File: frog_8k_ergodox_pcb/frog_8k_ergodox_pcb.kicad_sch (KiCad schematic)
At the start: 214 parts, among them J1 USB_C_Receptacle_USB2.0_14P, J10 Conn_01x01_Pin, J2 Conn_01x04_Pin, J3 Conn_01x01_Pin, J4 Conn_01x01_Pin, J5 Conn_01x01_Pin, J6 Conn_01x01_Pin, J7 Conn_01x01_Pin, J8 Conn_01x01_Pin, J9 Conn_01x01_Pin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

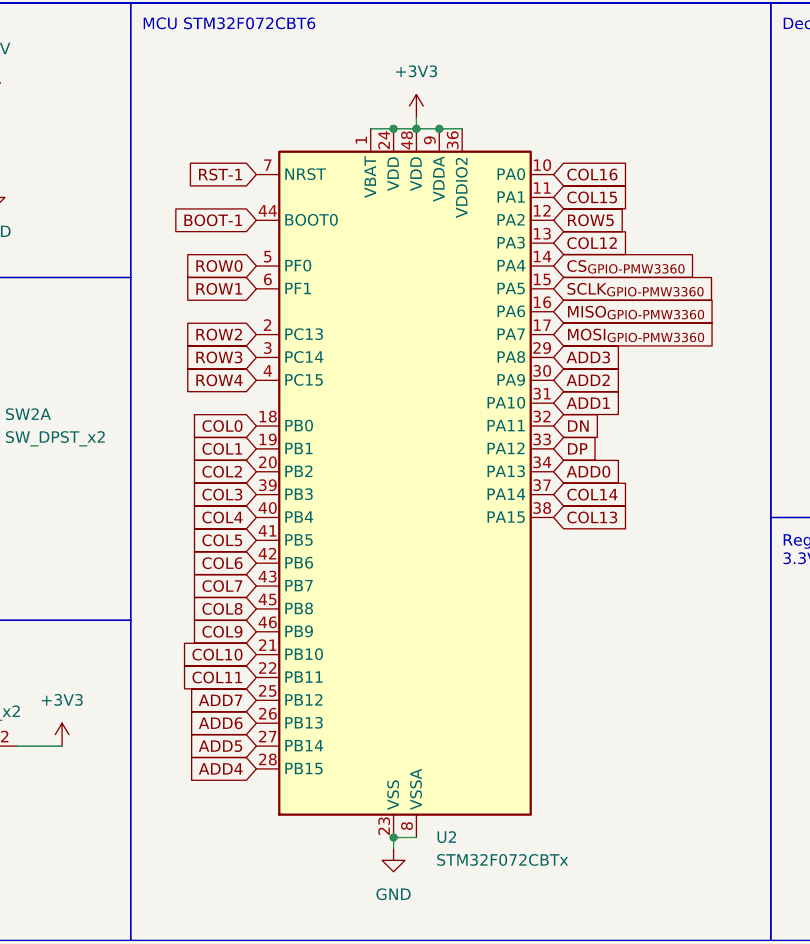
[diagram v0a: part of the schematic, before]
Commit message: Connected All nets.
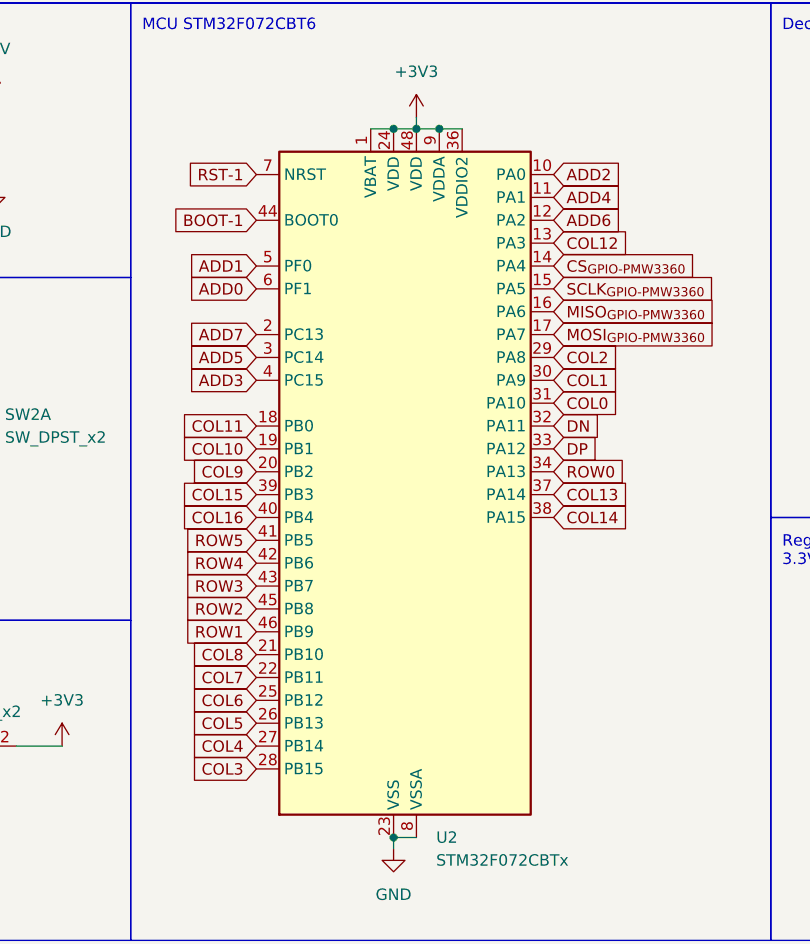
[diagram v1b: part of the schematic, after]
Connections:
- net ADD0: now also U2.6 (PF1); no longer U2.34 (PA13)
- net ADD1: now also U2.5 (PF0); no longer U2.31 (PA10)
- net ADD2: now also U2.10 (PA0); no longer U2.30 (PA9)
- net ADD3: now also U2.4 (PC15); no longer U2.29 (PA8)
- net ADD4: now also U2.11 (PA1); no longer U2.28 (PB15)
- net ADD5: now also U2.3 (PC14); no longer U2.27 (PB14)
- net ADD6: now also U2.12 (PA2); no longer U2.26 (PB13)
- net ADD7: now also U2.2 (PC13); no longer U2.25 (PB12)
- net COL0: now also U2.31 (PA10); no longer U2.18 (PB0)
- net COL1: now also U2.30 (PA9); no longer U2.19 (PB1)
- net COL10: now also U2.19 (PB1); no longer U2.21 (PB10)
- net COL11: now also U2.18 (PB0); no longer U2.22 (PB11)
- net COL13: now also U2.37 (PA14); no longer U2.38 (PA15)
- net COL14: now also U2.38 (PA15); no longer U2.37 (PA14)
- net COL15: now also U2.39 (PB3); no longer U2.11 (PA1)
- net COL16: now also U2.40 (PB4); no longer U2.10 (PA0)
- net COL2: now also U2.29 (PA8); no longer U2.20 (PB2)
- net COL3: now also U2.28 (PB15); no longer U2.39 (PB3)
- net COL4: now also U2.27 (PB14); no longer U2.40 (PB4)
- net COL5: now also U2.26 (PB13); no longer U2.41 (PB5)
- net COL6: now also U2.25 (PB12); no longer U2.42 (PB6)
- net COL7: now also U2.22 (PB11); no longer U2.43 (PB7)
- net COL8: now also U2.21 (PB10); no longer U2.45 (PB8)
- net COL9: now also U2.20 (PB2); no longer U2.46 (PB9)
- net ROW0: now also U2.34 (PA13); no longer U2.5 (PF0)
- net ROW1: now also U2.46 (PB9); no longer U2.6 (PF1)
- net ROW2: now also U2.45 (PB8); no longer U2.2 (PC13)
- net ROW3: now also U2.43 (PB7); no longer U2.3 (PC14)
- net ROW4: now also U2.42 (PB6); no longer U2.4 (PC15)
- net ROW5: now also U2.41 (PB5); no longer U2.12 (PA2)

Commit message: Almost Done with pcb
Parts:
- added R4: R1_10k, Resistor_SMD:R_0805_2012Metric_Pad1.20x1.40mm_HandSolder, symbol Device:R
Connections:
- no-connect marks 4 -> 6
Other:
- note added: "Additional Capacitor"
- note added: "Additional Resistor"
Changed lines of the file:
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@@
 	)
 	(no_connect
+		(at 326.39 77.47)
+	)
+	(no_connect
+		(at 334.01 77.47)
+	)
+	(no_connect
 		(at 270.51 261.62)
 	)
@@
 	)
 	(rectangle
+		(start 323.85 60.96)
+		(end 365.76 99.06)
+		(stroke
+			(width 0)
+			(type default)
+		)
+		(fill
+			(type none)
+		)
+	)
+	(rectangle
 		(start 212.09 237.49)
 		(end 299.72 284.48)
@@
 		)
 	)
+	(rectangle
+		(start 365.76 60.96)
+		(end 407.67 99.06)
+		(stroke
+			(width 0)
+			(type default)
+		)
+		(fill
+			(type none)
+		)
+	)
 	(text "TrackBall Housing\nMounting Hole, M2"
 		(exclude_from_sim no)
@@
 		)
 	)
+	(text "Additional Resistor"
+		(exclude_from_sim no)
+		(at 325.12 63.5 0)
+		(effects
+			(font
+				(size 1.27 1.27)
+			)
+			(justify left)
+		)
+	)
 	(text "MCU STM32F072CBT6"
 		(exclude_from_sim no)
@@
 		)
 	)
+	(text "Additional Capacitor"
+		(exclude_from_sim no)
+		(at 367.03 63.5 0)
+		(effects
+			(font
+				(size 1.27 1.27)
+			)
+			(justify left)
+		)
+	)
 	(text "Boot Switch\n"
 		(exclude_from_sim no)
@@
 					(unit 1)
 				)
+			)
+		)
+	)
+	(symbol
+		(lib_id "Device:R")
+		(at 330.2 77.47 90)
+		(unit 1)
+		(exclude_from_sim no)
+		(in_bom yes)
+		(on_board yes)
+		(dnp no)
+		(property "Reference" "R4"
+			(at 335.28 76.2 90)
+			(effects
+				(font
+					(size 1.27 1.27)
+				)
+				(justify right)
+			)
+		)
+		(property "Value" "R1_10k"
+			(at 335.28 78.74 90)
+			(effects
+				(font
+					(size 1.27 1.27)
+				)
+				(justify right)
+			)
+		)
+		(property "Footprint" "Resistor_SMD:R_0805_2012Metric_Pad1.20x1.40mm_HandSolder"
+			(at 330.2 79.248 90)
+			(effects
+				(font
+					(size 1.27 1.27)
+				)
+				(hide yes)
+			)
+		)
+		(property "Datasheet" "~"
+			(at 330.2 77.47 0)
+			(effects
+				(font
+					(size 1.27 1.27)
+				)
+				(hide yes)
+			)
+		)
+		(property "Description" "Resistor"
+			(at 330.2 77.47 0)
+			(effects
+				(font
+					(size 1.27 1.27)
+				)
+				(hide yes)
+			)
+		)
+		(pin "1"
+		)
+		(pin "2"
+		)
+		(instances
+			(project "frog_8k_ergodox_pcb"
+				(path "/34ddd234-11af-4a66-9186-ea72bce9a0a9"
+					(reference "R4")
+					(unit 1)
+				)
